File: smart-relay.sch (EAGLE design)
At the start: 13 parts, among them U1 RFD22301

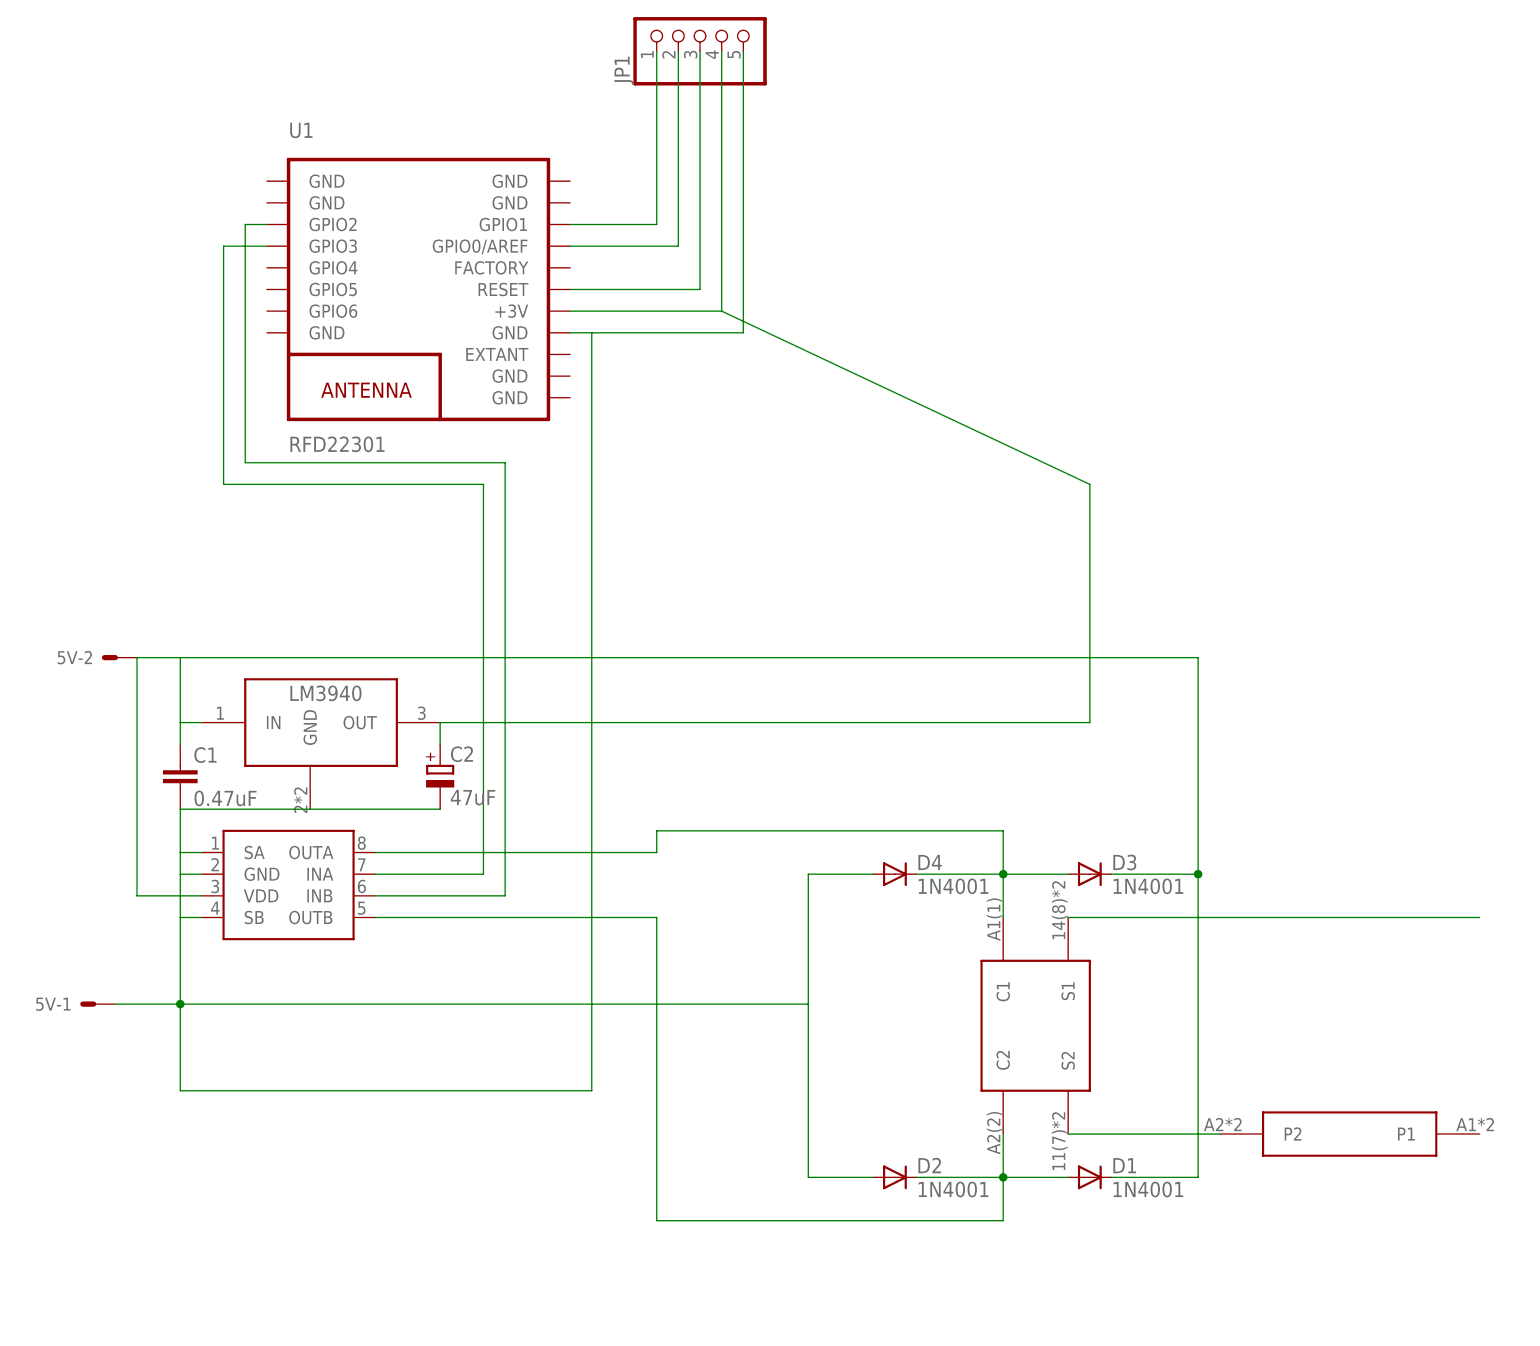
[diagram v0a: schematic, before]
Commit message: Added LED and moved trace outside of bluetooth.
* Added a bicolor LED in parallel with the relay coil to make debugging
  easier.
* Moved trace from under rfd22301 place so the PCB can be cut and the
  rfd22301 can pe soldered in line with the rest of the PCB. Removing
  the rfd22301 will be easier this way.
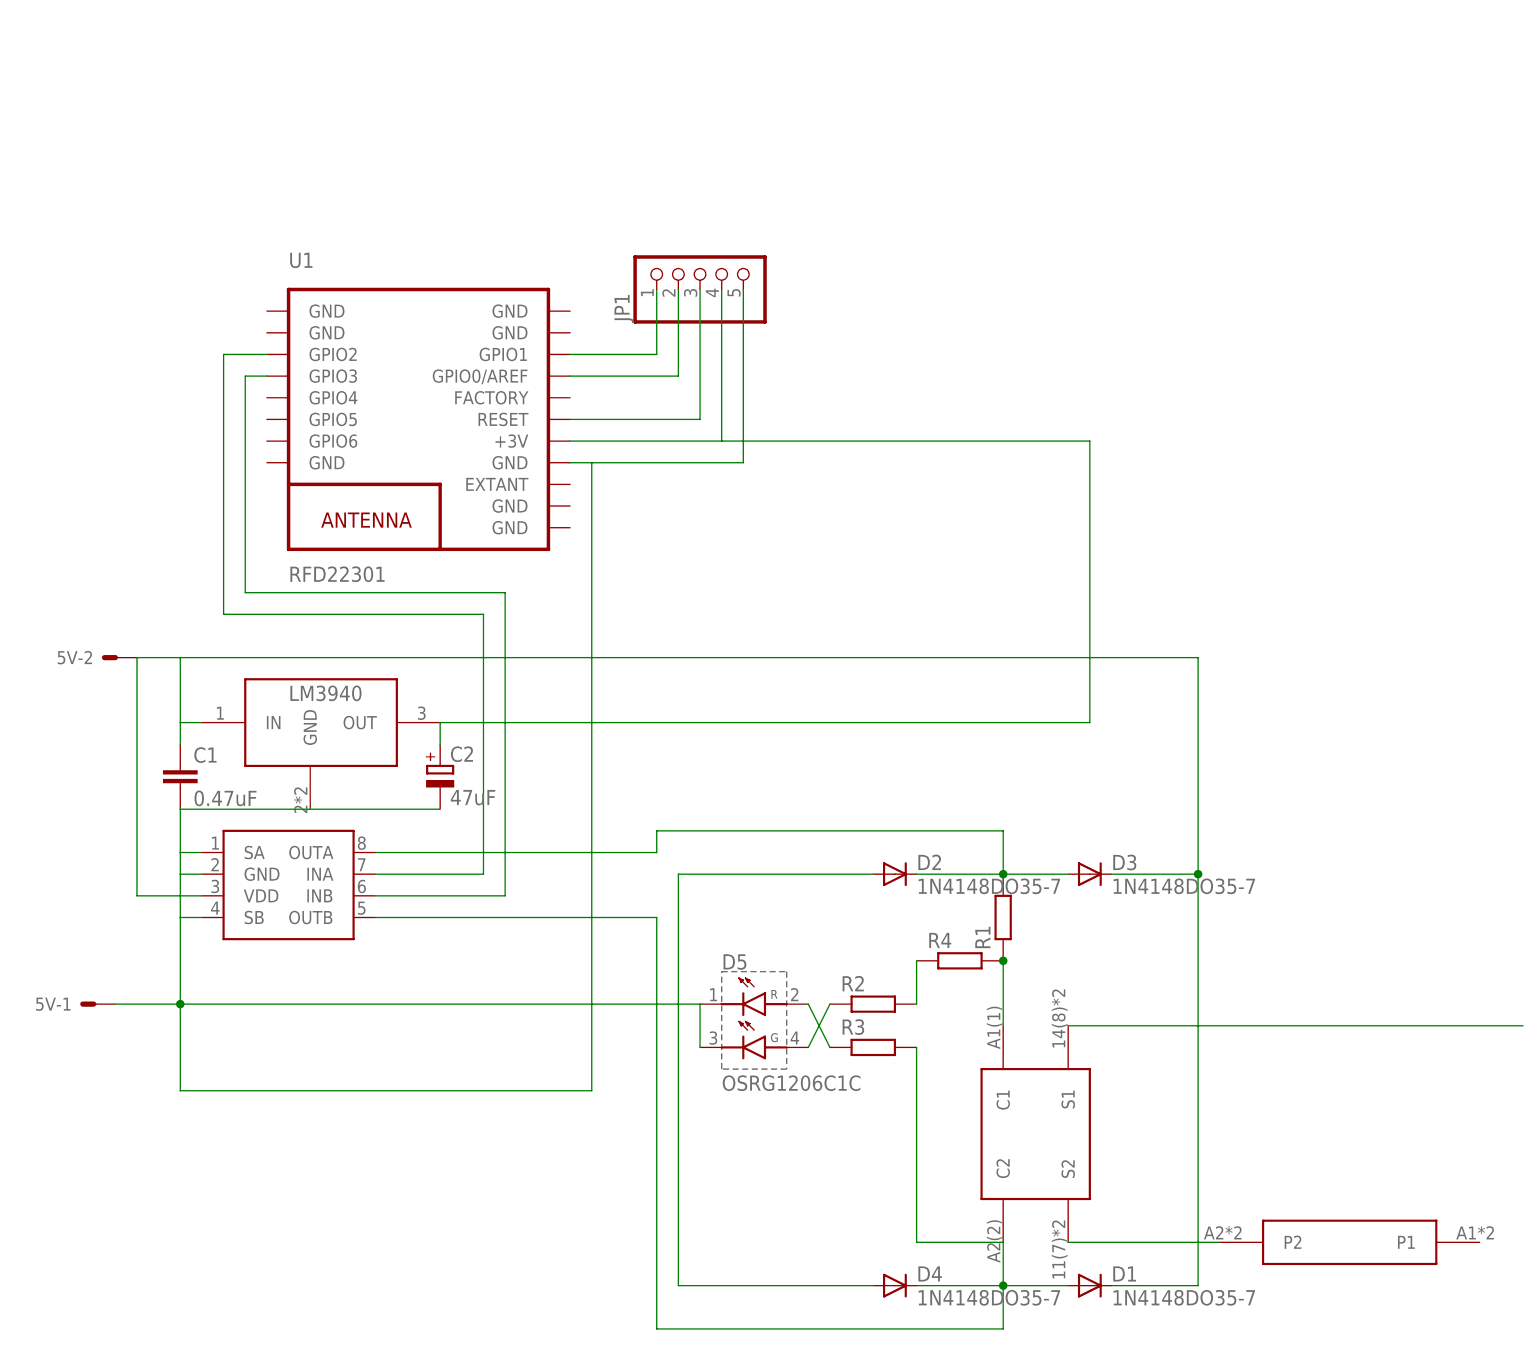
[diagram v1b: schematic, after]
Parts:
- added D5: OSRG1206C1C, something:OSRG1206C1C
- added R1: (no value), rcl:R-EU_0204/2V
- added R2, R3: (no value), eagle-ltspice:RR1206
- added R4: (no value), rcl:R-EU_0204/5
- D1, D2, D3, D4: value 1N4001 -> 1N4148DO35-7; device diode:1N4004 -> diode:1N4148DO35-7
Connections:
- new net N$13: R1.1, R4.2, U$1.C1
- new net N$14: R2.2, R4.1
- new net N$15: D5.4, R2.1
- new net N$16: D5.2, R3.1
- net N$10: now also D4.C, R3.2; no longer D2.C
- net N$4: now also U1.GPIO2; no longer U1.GPIO3
- net N$5: now also U1.GPIO3; no longer U1.GPIO2
- net N$7: now also D5.1, D5.3
- net N$9: now also D2.C, R1.2; no longer D4.C, U$1.C1
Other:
- moved on the sheet: JP1, U1
